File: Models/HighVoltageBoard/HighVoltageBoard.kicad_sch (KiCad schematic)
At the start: 0 parts

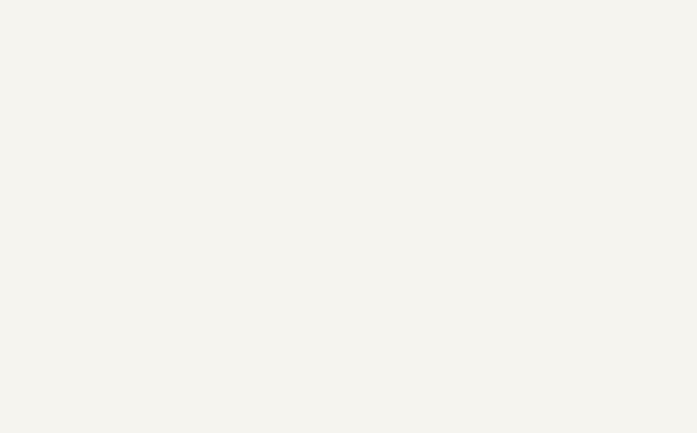
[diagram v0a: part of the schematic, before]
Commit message: Added mounting holes
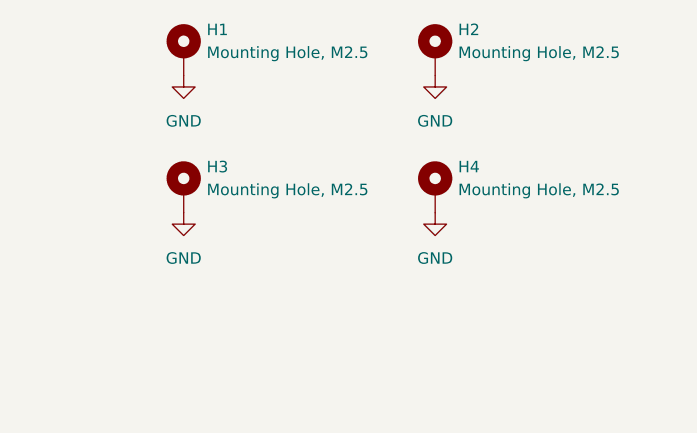
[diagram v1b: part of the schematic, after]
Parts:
- added H1, H2, H3, H4: Mounting Hole, M2.5, MountingHole:MountingHole_2.7mm_M2.5_DIN965_Pad, symbol Mechanical:MountingHole_Pad
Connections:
- new net GND: H1.1, H2.1, H3.1, H4.1

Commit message: Save progress
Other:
- note removed: "inputs: up to ±12 V outputs: up to approx. ∓430 V power cords received: 450 V, GND, -450 V"
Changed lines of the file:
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@@
-		)
-	)
-	(text "inputs: up to ±12 V\noutputs: up to approx. ∓430 V\npower cords received: 450 V, GND, -450 V"
-		(exclude_from_sim no)
-		(at 102.362 26.924 0)
-		(effects
-			(font
-				(size 1.27 1.27)
-			)
-			(justify left top)
 		)
 	)

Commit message: Save progress
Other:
- note added: "IN/SENSEN receptacle type: pin/socket connections output voltage receptacle type: (1) SMA with RG-58/U for 500V rating (2) 1x3 pin socket, GND + OUT + OUT GND interface to other boards: many pin/socket connections"
- note removed: "IN/SENSEN receptacle type: pin/socket connections output voltage receptacle type: (1) SMA with 500V rating and RG-58/U (2) 1x3 pin socket, GND + OUT + OUT GND interface to other boards: many pin/socket connections"
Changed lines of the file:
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@@
 	(generator_version "9.0")
 	(paper "A4")
-	(text "IN/SENSEN receptacle type:\npin/socket connections\n\noutput voltage receptacle type:\n(1) SMA with 500V rating and RG-58/U\n(2) 1x3 pin socket, GND + OUT + OUT\n\nGND interface to other boards:\nmany pin/socket connections"
+	(text "IN/SENSEN receptacle type:\npin/socket connections\n\noutput voltage receptacle type:\n(1) SMA with RG-58/U for 500V rating\n(2) 1x3 pin socket, GND + OUT + OUT\n\nGND interface to other boards:\nmany pin/socket connections"
 		(exclude_from_sim no)
 		(at 27.178 26.924 0)

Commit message: Save progress
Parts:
- added J12: Conn_01x13_Socket, symbol Connector:Conn_01x13_Socket
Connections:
- net GND: now also J12.1 (Pin_1), J12.10 (Pin_10), J12.13 (Pin_13), J12.4 (Pin_4), J12.7 (Pin_7)
- net INA: now also J12.3 (Pin_3)
- net INB: now also J12.6 (Pin_6)
- net INC: now also J12.9 (Pin_9)
- net IND: now also J12.12 (Pin_12)
- net SENSENA: now also J12.2 (Pin_2)
- net SENSENB: now also J12.5 (Pin_5)
- net SENSENC: now also J12.8 (Pin_8)
- net SENSEND: now also J12.11 (Pin_11)

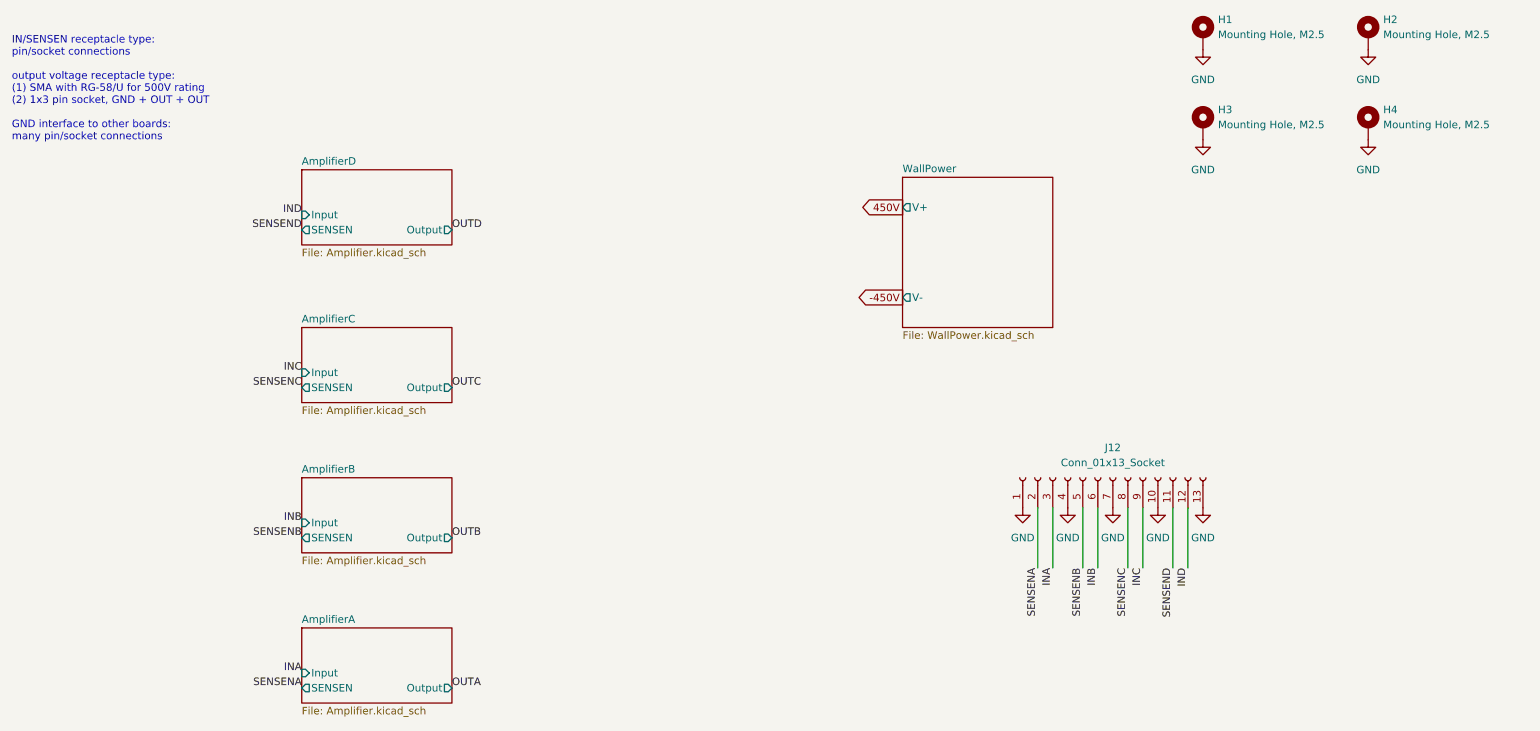
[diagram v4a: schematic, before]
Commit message: Connectors should be fully specified now
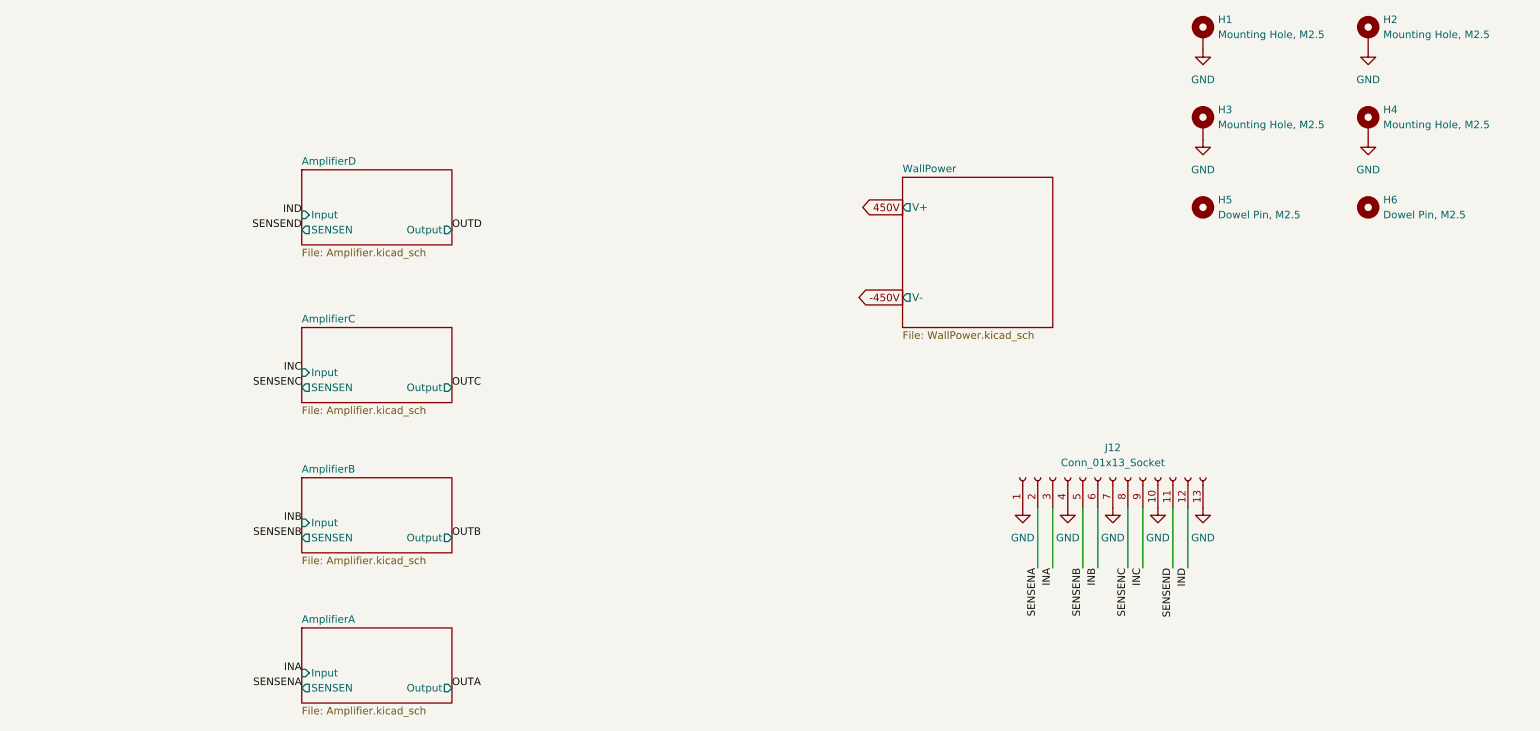
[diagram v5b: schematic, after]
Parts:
- added H5, H6: Dowel Pin, M2.5, symbol Mechanical:MountingHole
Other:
- note removed: "IN/SENSEN receptacle type: pin/socket connections output voltage receptacle type: (1) SMA with RG-58/U for 500V rating (2) 1x3 pin socket, GND + OUT + OUT GND interface to other boards: many pin/socket connections"
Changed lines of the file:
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@@
 	(generator_version "9.0")
 	(paper "A4")
-	(text "IN/SENSEN receptacle type:\npin/socket connections\n\noutput voltage receptacle type:\n(1) SMA with RG-58/U for 500V rating\n(2) 1x3 pin socket, GND + OUT + OUT\n\nGND interface to other boards:\nmany pin/socket connections"
-		(exclude_from_sim no)
-		(at 27.178 26.924 0)
-		(effects
-			(font
-				(size 1.27 1.27)
-			)
-			(justify left top)
-		)
-	)
 	(wire
 		(pts
@@
 	)
 	(symbol
+		(lib_id "Mechanical:MountingHole")
+		(at 256.54 55.88 0)
+		(unit 1)
+		(exclude_from_sim no)
+		(in_bom no)
+		(on_board yes)
+		(dnp no)
+		(fields_autoplaced yes)
+		(property "Reference" "H6"
+			(at 259.08 54.6099 0)
+			(effects
+				(font
+					(size 1.27 1.27)
+				)
+				(justify left)
+			)
+		)
+		(property "Value" "Dowel Pin, M2.5"
+			(at 259.08 57.1499 0)
+			(effects
+				(font
+					(size 1.27 1.27)
+				)
+				(justify left)
+			)
+		)
+		(property "Footprint" ""
+			(at 256.54 55.88 0)
+			(effects
+				(font
+					(size 1.27 1.27)
+				)
+				(hide yes)
+			)
+		)
+		(property "Datasheet" "~"
+			(at 256.54 55.88 0)
+			(effects
+				(font
+					(size 1.27 1.27)
+				)
+				(hide yes)
+			)
+		)
+		(property "Description" "Mounting Hole without connection"
+			(at 256.54 55.88 0)
+			(effects
+				(font
+					(size 1.27 1.27)
+				)
+				(hide yes)
+			)
+		)
+		(property "Purchase Link" ""
+			(at 256.54 55.88 0)
+			(effects
+				(font
+					(size 1.27 1.27)
+				)
+				(hide yes)
+			)
+		)
+		(instances
+			(project "HighVoltageBoard"
+				(path "/c83b09c9-14ae-4b68-b7fa-4c89bba29dc5"
+					(reference "H6")
+					(unit 1)
+				)
+			)
+		)
+	)
+	(symbol
 		(lib_id "Mechanical:MountingHole_Pad")
 		(at 256.54 26.67 0)
@@
 					(unit 1)
 				)
+			)
+		)
+	)
+	(symbol
+		(lib_id "Mechanical:MountingHole")
+		(at 228.6 55.88 0)
+		(unit 1)
+		(exclude_from_sim no)
+		(in_bom no)
+		(on_board yes)
+		(dnp no)
+		(fields_autoplaced yes)
+		(property "Reference" "H5"
+			(at 231.14 54.6099 0)
+			(effects
+				(font
+					(size 1.27 1.27)
+				)
+				(justify left)
+			)
+		)
+		(property "Value" "Dowel Pin, M2.5"
+			(at 231.14 57.1499 0)
+			(effects
+				(font
+					(size 1.27 1.27)
+				)
+				(justify left)
+			)
+		)
+		(property "Footprint" ""
+			(at 228.6 55.88 0)
+			(effects
+				(font
+					(size 1.27 1.27)
+				)
+				(hide yes)
+			)
+		)
+		(property "Datasheet" "~"
+			(at 228.6 55.88 0)
+			(effects
+				(font
+					(size 1.27 1.27)
+				)
+				(hide yes)
+			)
+		)
+		(property "Description" "Mounting Hole without connection"
+			(at 228.6 55.88 0)
+			(effects
+				(font
+					(size 1.27 1.27)
+				)
+				(hide yes)
+			)
+		)
+		(property "Purchase Link" ""
+			(at 228.6 55.88 0)
+			(effects
+				(font
+					(size 1.27 1.27)
+				)
+				(hide yes)
+			)
+		)
+		(instances
+			(project "HighVoltageBoard"
+				(path "/c83b09c9-14ae-4b68-b7fa-4c89bba29dc5"
+					(reference "H5")
+					(unit 1)
+				)

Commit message: Passes ERC
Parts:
- renumbered H3 to H2, H5 to H3, H2 to H4, H4 to H5, J12 to J1
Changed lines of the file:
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@@
 		(dnp no)
 		(fields_autoplaced yes)
-		(property "Reference" "#PWR029"
+		(property "Reference" "#PWR06"
 			(at 228.6 50.8 0)
 			(effects
@@
 			(project "HighVoltageBoard"
 				(path "/c83b09c9-14ae-4b68-b7fa-4c89bba29dc5"
-					(reference "#PWR029")
+					(reference "#PWR06")
 					(unit 1)
 				)
@@
 		(dnp no)
 		(fields_autoplaced yes)
-		(property "Reference" "J12"
+		(property "Reference" "J1"
 			(at 213.36 96.52 90)
 			(effects
@@
 			(project ""
 				(path "/c83b09c9-14ae-4b68-b7fa-4c89bba29dc5"
-					(reference "J12")
+					(reference "J1")
 					(unit 1)
 				)
@@
 		(dnp no)
 		(fields_autoplaced yes)
-		(property "Reference" "H2"
+		(property "Reference" "H4"
 			(at 259.08 24.1299 0)
 			(effects
@@
 			(project "HighVoltageBoard"
 				(path "/c83b09c9-14ae-4b68-b7fa-4c89bba29dc5"
-					(reference "H2")
+					(reference "H4")
 					(unit 1)
 				)
@@
 		(dnp no)
 		(fields_autoplaced yes)
-		(property "Reference" "#PWR036"
+		(property "Reference" "#PWR03"
 			(at 213.36 113.03 0)
 			(effects
@@
 			(project "HighVoltageBoard"
 				(path "/c83b09c9-14ae-4b68-b7fa-4c89bba29dc5"
-					(reference "#PWR036")
+					(reference "#PWR03")
 					(unit 1)
 				)
@@
 		(dnp no)
 		(fields_autoplaced yes)
-		(property "Reference" "H5"
+		(property "Reference" "H3"
 			(at 231.14 54.6099 0)
 			(effects
@@
 			(project "HighVoltageBoard"
 				(path "/c83b09c9-14ae-4b68-b7fa-4c89bba29dc5"
-					(reference "H5")
+					(reference "H3")
 					(unit 1)
 				)
@@
 		(dnp no)
 		(fields_autoplaced yes)
-		(property "Reference" "H3"
+		(property "Reference" "H2"
 			(at 231.14 39.3699 0)
 			(effects
@@
 			(project "HighVoltageBoard"
 				(path "/c83b09c9-14ae-4b68-b7fa-4c89bba29dc5"
-					(reference "H3")
+					(reference "H2")
 					(unit 1)
 				)
@@
 		(dnp no)
 		(fields_autoplaced yes)
-		(property "Reference" "#PWR038"
+		(property "Reference" "#PWR07"
 			(at 228.6 113.03 0)
 			(effects
@@
 			(project "HighVoltageBoard"
 				(path "/c83b09c9-14ae-4b68-b7fa-4c89bba29dc5"
-					(reference "#PWR038")
+					(reference "#PWR07")
 					(unit 1)
 				)
@@
 		(dnp no)
 		(fields_autoplaced yes)
-		(property "Reference" "#PWR037"
+		(property "Reference" "#PWR04"
 			(at 220.98 113.03 0)
 			(effects
@@
 			(project "HighVoltageBoard"
 				(path "/c83b09c9-14ae-4b68-b7fa-4c89bba29dc5"
-					(reference "#PWR037")
+					(reference "#PWR04")
 					(unit 1)
 				)
@@
 		(dnp no)
 		(fields_autoplaced yes)
-		(property "Reference" "#PWR035"
+		(property "Reference" "#PWR02"
 			(at 205.74 113.03 0)
 			(effects
@@
 			(project "HighVoltageBoard"
 				(path "/c83b09c9-14ae-4b68-b7fa-4c89bba29dc5"
-					(reference "#PWR035")
+					(reference "#PWR02")
 					(unit 1)
 				)
@@
 		(dnp no)
 		(fields_autoplaced yes)
-		(property "Reference" "#PWR028"
+		(property "Reference" "#PWR08"
 			(at 256.54 35.56 0)
 			(effects
@@
 			(project "HighVoltageBoard"
 				(path "/c83b09c9-14ae-4b68-b7fa-4c89bba29dc5"
-					(reference "#PWR028")
+					(reference "#PWR08")
 					(unit 1)
 				)
@@
 		(dnp no)
 		(fields_autoplaced yes)
-		(property "Reference" "#PWR034"
+		(property "Reference" "#PWR01"
 			(at 198.12 113.03 0)
 			(effects
@@
 			(project ""
 				(path "/c83b09c9-14ae-4b68-b7fa-4c89bba29dc5"
-					(reference "#PWR034")
+					(reference "#PWR01")
 					(unit 1)
 				)
@@
 		(dnp no)
 		(fields_autoplaced yes)
-		(property "Reference" "#PWR027"
+		(property "Reference" "#PWR05"
 			(at 228.6 35.56 0)
 			(effects
@@
 			(project "HighVoltageBoard"
 				(path "/c83b09c9-14ae-4b68-b7fa-4c89bba29dc5"
-					(reference "#PWR027")
+					(reference "#PWR05")
 					(unit 1)
 				)
@@
 		(dnp no)
 		(fields_autoplaced yes)
-		(property "Reference" "#PWR030"
+		(property "Reference" "#PWR09"
 			(at 256.54 50.8 0)
 			(effects
@@
 			(project "HighVoltageBoard"
 				(path "/c83b09c9-14ae-4b68-b7fa-4c89bba29dc5"
-					(reference "#PWR030")
+					(reference "#PWR09")
 					(unit 1)
 				)
@@
 		(dnp no)
 		(fields_autoplaced yes)
-		(property "Reference" "H4"
+		(property "Reference" "H5"
 			(at 259.08 39.3699 0)
 			(effects
@@
 			(project "HighVoltageBoard"
 				(path "/c83b09c9-14ae-4b68-b7fa-4c89bba29dc5"
-					(reference "H4")
-					(unit 1)
-				)
+					(reference "H5")
+					(unit 1)
+				)

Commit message: Save progress
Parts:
- J1: Cost $0.76 -> $0.760
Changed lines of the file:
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@@
 			)
 		)
-		(property "Cost" "$0.76"
+		(property "Cost" "$0.760"
 			(at 213.36 101.6 90)
 			(effects

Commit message: Assigned footprints
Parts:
- H1, H2, H4, H5: footprint MountingHole:MountingHole_2.7mm_M2.5_DIN965_Pad -> Connector_Custom:Keystone_24929
- H3, H6: footprint (none) -> Connector_Custom:DowelPin_2.5mm
- J1: footprint (none) -> Connector_Custom:PinConnector_1x13
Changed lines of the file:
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@@
 			)
 		)
-		(property "Footprint" ""
+		(property "Footprint" "Connector_Custom:PinConnector_1x13"
 			(at 213.36 101.6 0)
 			(effects
@@
 			)
 		)
-		(property "Footprint" ""
+		(property "Footprint" "Connector_Custom:DowelPin_2.5mm"
 			(at 256.54 55.88 0)
 			(effects
@@
 			)
 		)
-		(property "Footprint" "MountingHole:MountingHole_2.7mm_M2.5_DIN965_Pad"
+		(property "Footprint" "Connector_Custom:Keystone_24929"
 			(at 256.54 26.67 0)
 			(effects
@@
 			)
 		)
-		(property "Footprint" ""
+		(property "Footprint" "Connector_Custom:DowelPin_2.5mm"
 			(at 228.6 55.88 0)
 			(effects
@@
 			)
 		)
-		(property "Footprint" "MountingHole:MountingHole_2.7mm_M2.5_DIN965_Pad"
+		(property "Footprint" "Connector_Custom:Keystone_24929"
 			(at 228.6 41.91 0)
 			(effects
@@
 			)
 		)
-		(property "Footprint" "MountingHole:MountingHole_2.7mm_M2.5_DIN965_Pad"
+		(property "Footprint" "Connector_Custom:Keystone_24929"
 			(at 228.6 26.67 0)
 			(effects
@@
 			)
 		)
-		(property "Footprint" "MountingHole:MountingHole_2.7mm_M2.5_DIN965_Pad"
+		(property "Footprint" "Connector_Custom:Keystone_24929"
 			(at 256.54 41.91 0)
 			(effects
